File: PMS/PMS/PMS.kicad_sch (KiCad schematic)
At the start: 36 parts, among them IC1 TMCS1107A1BQDRQ1, IC2 ADR3450ARJZ-R7, IC3 TL2575-12IKTTR, J1 XT60PW-M, J2 XT60PW-F, J3 XT60PW-M, J4 XT60PW-F, J5 XT60PW-F, J6 Conn_01x02_Male, U1 ADC101C027CIMK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

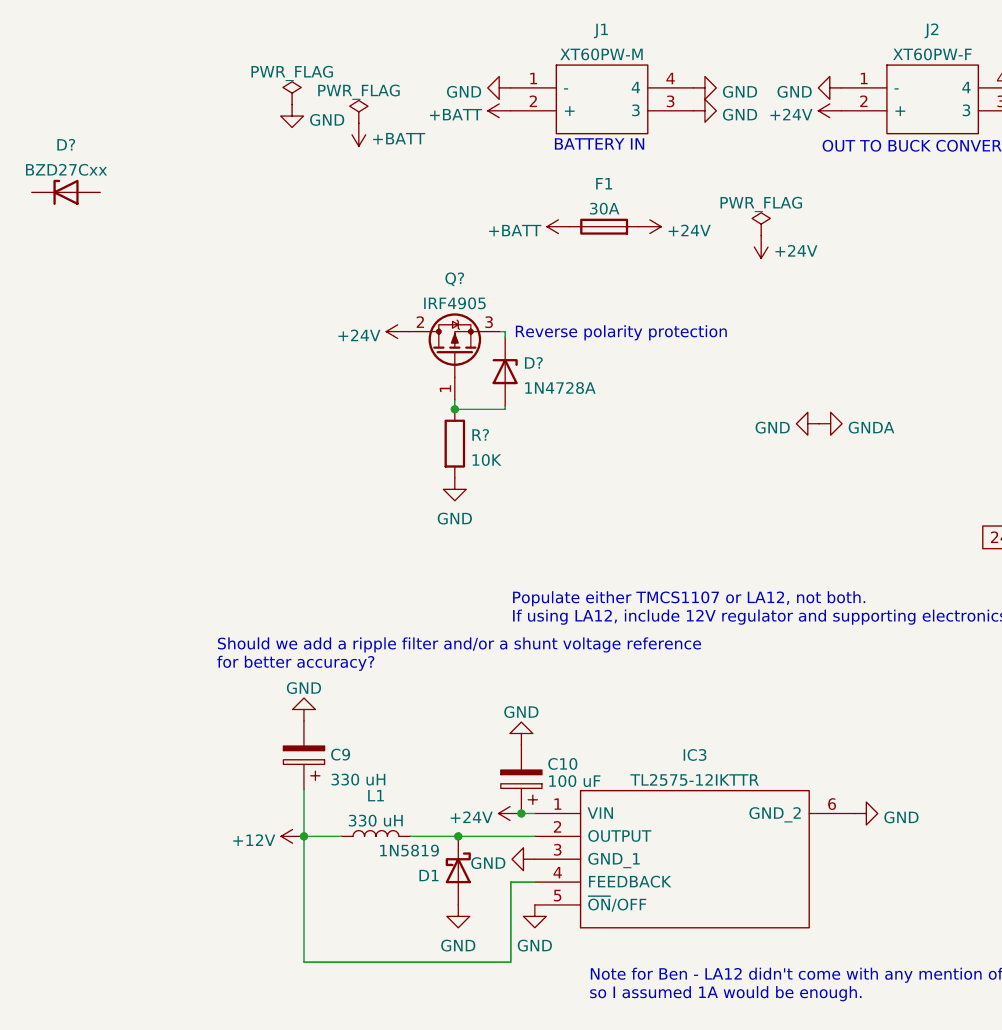
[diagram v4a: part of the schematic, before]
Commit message: cleanup and now ERC compliant
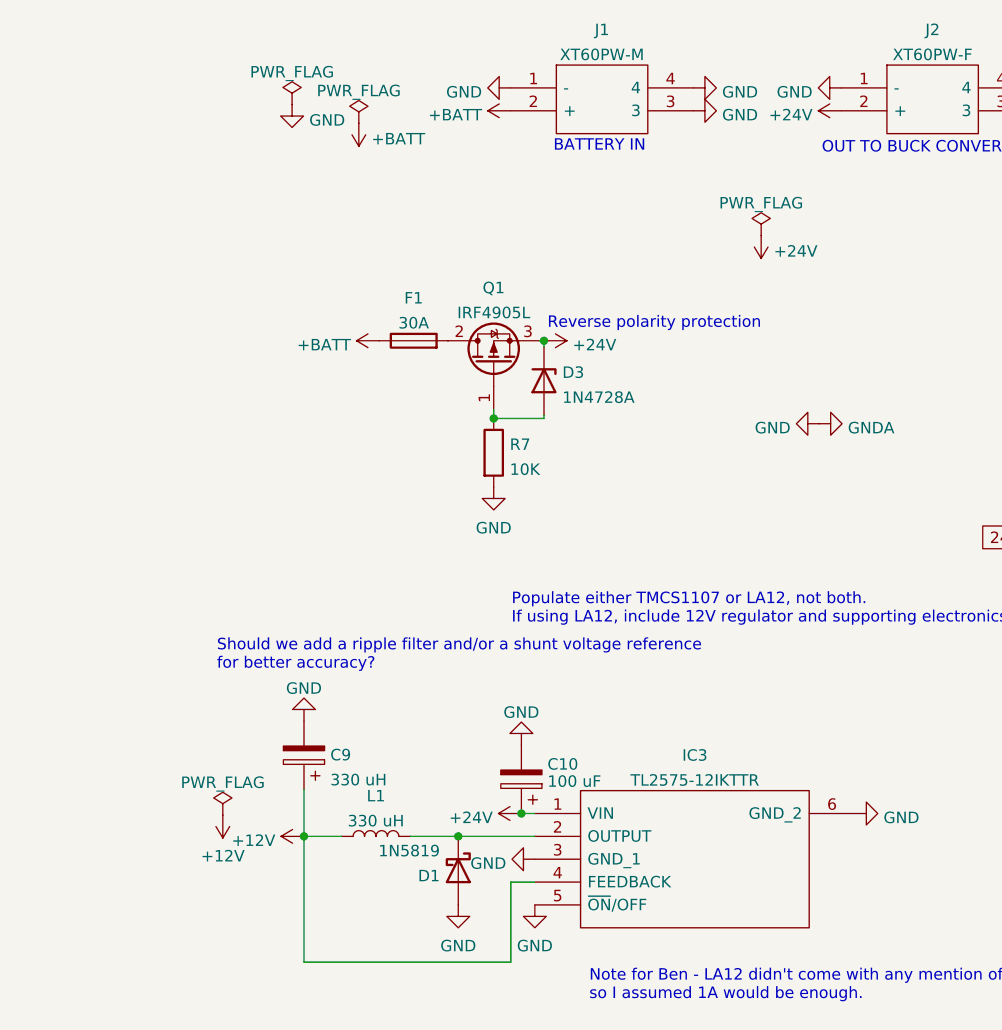
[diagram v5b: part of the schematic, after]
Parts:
- removed D?: BZD27Cxx, Diode_SMD:D_SMF, symbol Diode:BZD27Cxx
- Q1: renamed from Q?; value IRF4905 -> IRF4905L; footprint Package_TO_SOT_THT:TO-220-3_Vertical -> Package_TO_SOT_THT:TO-262-3-1EP_Horizontal_TabDown
- gave numbers to parts that had none: 2
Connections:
- net +24V: now also D3.1 (K), Q1.3 (S); no longer F1.2, Q1.2 (D)
- new net: F1.2, Q1.2 (D)
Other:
- moved on the sheet: D3, F1, Q1, R7

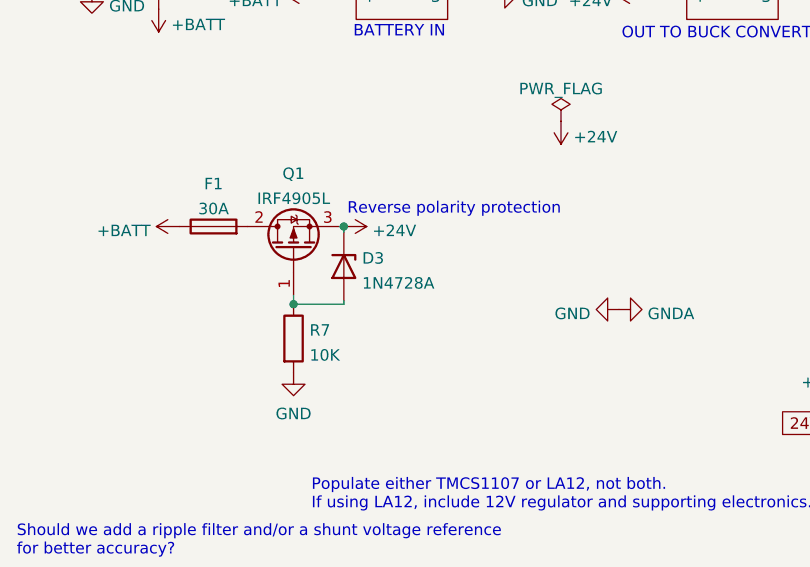
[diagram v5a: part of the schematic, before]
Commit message: switched to the correct zener diode
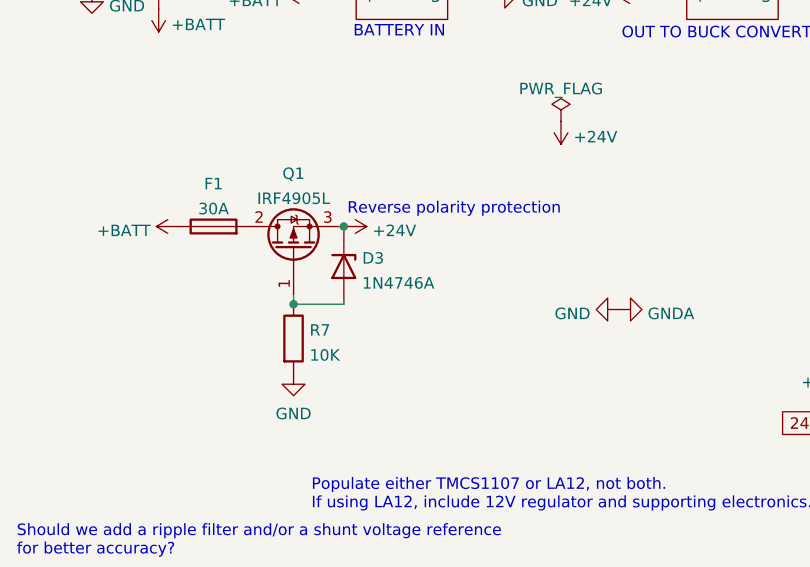
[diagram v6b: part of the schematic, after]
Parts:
- D3: value 1N4728A -> 1N4746A
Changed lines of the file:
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@@
       (effects (font (size 1.27 1.27)) (justify left))
     )
-    (property "Value" "1N4728A" (id 1) (at 58.42 66.6366 90)
+    (property "Value" "1N4746A" (id 1) (at 58.42 66.6366 90)
       (effects (font (size 1.27 1.27)) (justify left))
     )
@@
     )
     (path "/8c58b9c6-42fa-43ad-a456-e387b2c947c3"
-      (reference "D3") (unit 1) (value "1N4728A") (footprint "Diode_THT:D_DO-41_SOD81_P10.16mm_Horizontal")
+      (reference "D3") (unit 1) (value "1N4746A") (footprint "Diode_THT:D_DO-41_SOD81_P10.16mm_Horizontal")
     )
     (path "/f7d7bb3d-3174-4f8d-bddb-cbcecab3f605"

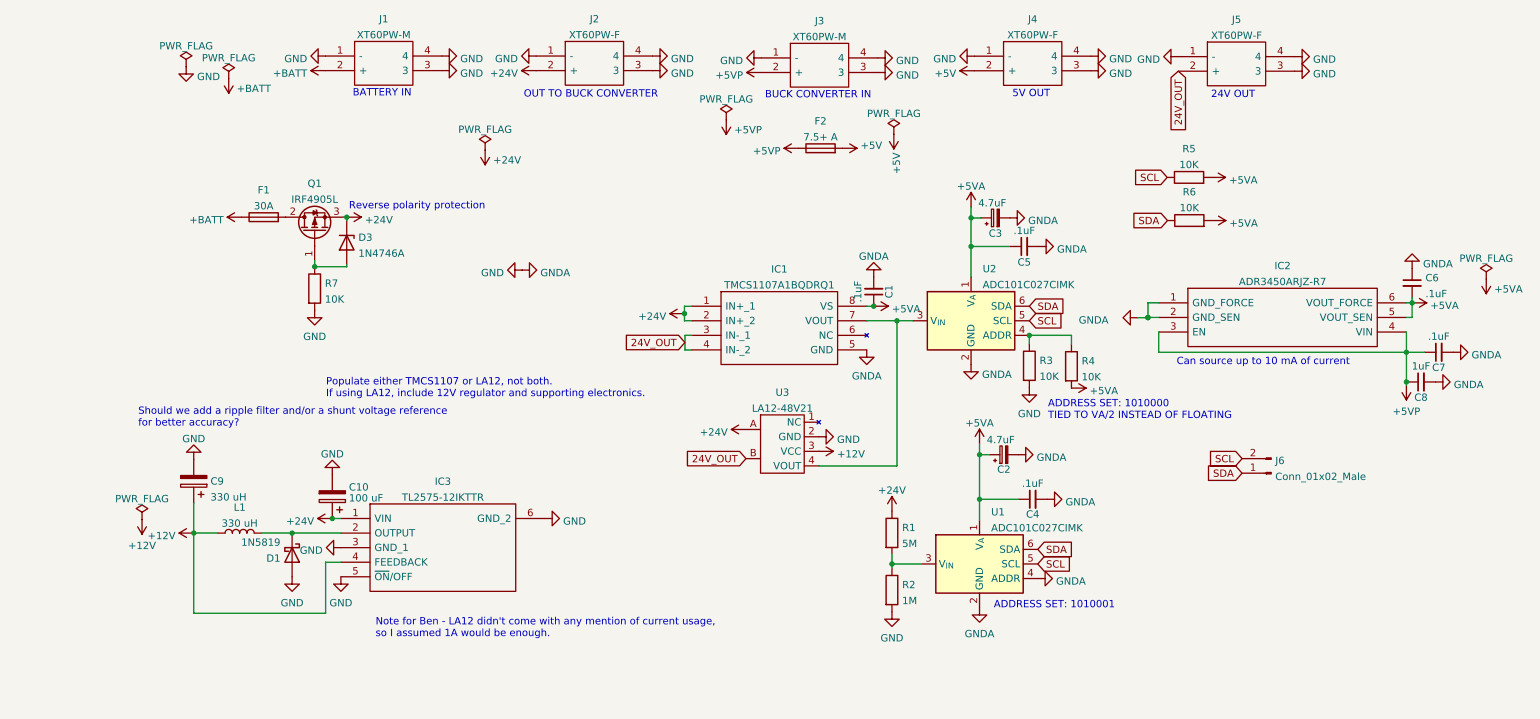
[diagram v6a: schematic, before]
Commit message: Associated footprints to components
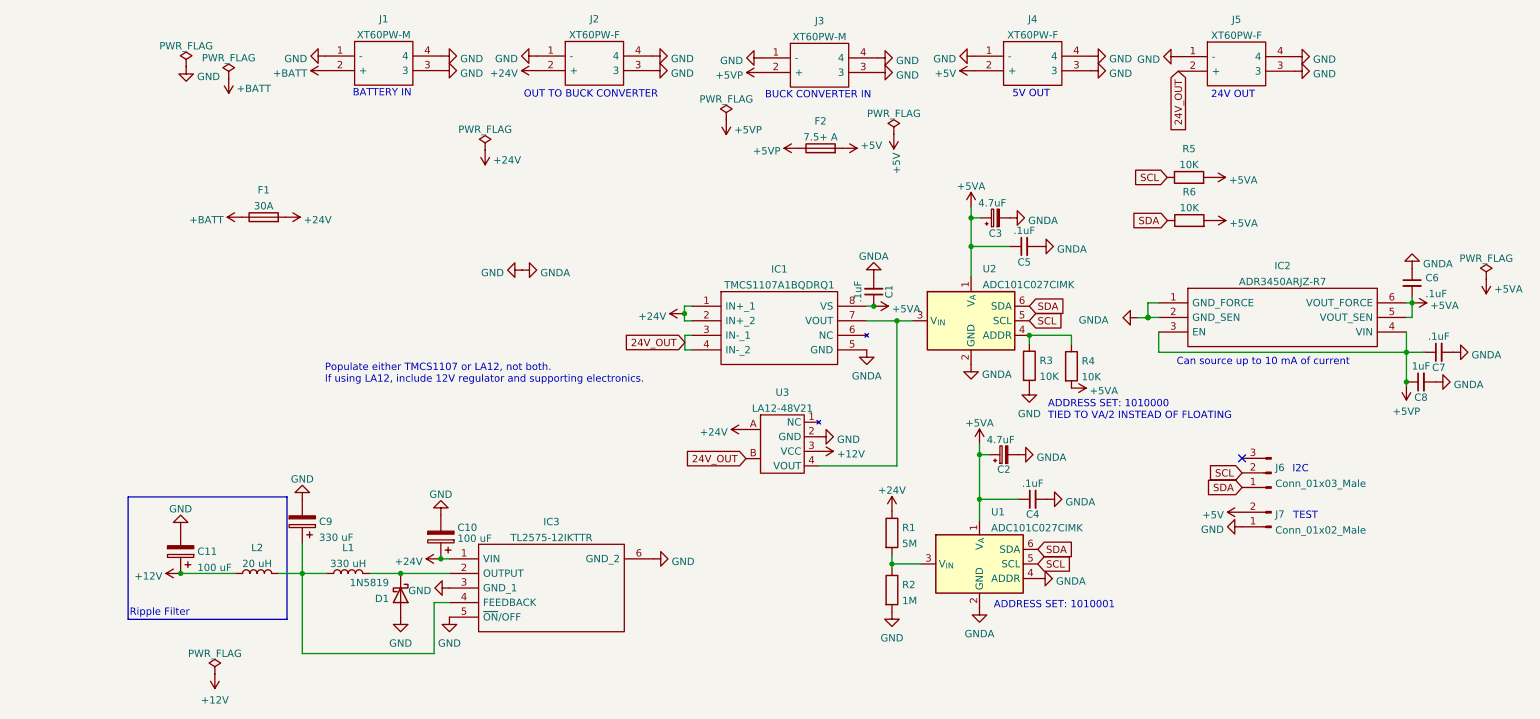
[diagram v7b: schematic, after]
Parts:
- removed D3: 1N4746A, Diode_THT:D_DO-41_SOD81_P10.16mm_Horizontal, symbol Diode:1N47xxA
- removed J6: Conn_01x02_Male, Connector_Molex:Molex_KK-254_AE-6410-02A_1x02_P2.54mm_Vertical, symbol Connector:Conn_01x02_Male
- removed Q1: IRF4905L, Package_TO_SOT_THT:TO-262-3-1EP_Horizontal_TabDown, symbol Transistor_FET:IRF4905
- removed R7: 10K, symbol Device:R
- added C11: 100 uF, Capacitor_SMD:CP_Elec_10x10.5, symbol Device:C_Polarized
- added J6: Conn_01x03_Male, Connector_JST:JST_XH_B3B-XH-AM_1x03_P2.50mm_Vertical, symbol Connector:Conn_01x03_Male
- added J7: Conn_01x02_Male, Connector_JST:JST_XH_B2B-XH-AM_1x02_P2.50mm_Vertical, symbol Connector:Conn_01x02_Male
- added L2: 20 uH, Inductor_SMD:L_Bourns_SRN6045TA, symbol Device:L
- C1, C4, C5, C6, C7, C8: footprint (none) -> Capacitor_SMD:C_0805_2012Metric_Pad1.18x1.45mm_HandSolder
- C10: footprint (none) -> Capacitor_SMD:CP_Elec_10x10.5
- C2, C3: footprint (none) -> Capacitor_Tantalum_SMD:CP_EIA-3216-18_Kemet-A_Pad1.58x1.35mm_HandSolder
- C9: value 330 uH -> 330 uF; footprint (none) -> Capacitor_SMD:CP_Elec_8x6.5
- F1, F2: footprint (none) -> LIB_3576:3576
- L1: footprint (none) -> Inductor_SMD:L_Bourns_SRR1210A
- R1, R2, R3, R4, R5, R6: footprint (none) -> Resistor_SMD:R_0805_2012Metric_Pad1.20x1.40mm_HandSolder
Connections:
- net +12V: now also C11.1, L2.1; no longer C9.1, IC3.4 (FEEDBACK), L1.1
- net +24V: now also F1.2
- net +5V: now also J7.2 (Pin_2)
- net GND: now also C11.2, J7.1 (Pin_1)
- net SCL: now also J6.2 (Pin_2)
- net SDA: now also J6.1 (Pin_1)
- new net: C9.1, IC3.4 (FEEDBACK), L1.1, L2.2
- no-connect marks 0 -> 1
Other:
- note added: "I2C"
- note added: "Ripple Filter"
- note added: "TEST"
- note removed: "Note for Ben - LA12 didn't come with any mention of current usage, so I assumed 1A would be enough."
- note removed: "Reverse polarity protection"
- note removed: "Should we add a ripple filter and/or a shunt voltage reference for better accuracy?"
- moved on the sheet: C10, C9, D1, IC3, L1

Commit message: adding BOM PMS.csv
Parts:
- added J8: Conn_01x02_Male, Connector_JST:JST_XH_B2B-XH-AM_1x02_P2.50mm_Vertical, symbol Connector:Conn_01x02_Male
- C1, C4, C5, C6, C7: DigiKey Part Number (none) -> 399-C0805C104M5RAC7800TR-ND
- C10, C11: DigiKey Part Number (none) -> 399-EDK107M025A9LAATR-ND
- C2, C3: DigiKey Part Number (none) -> 399-3696-1-ND
- C8: DigiKey Part Number (none) -> 399-15436-2-ND
- C9: DigiKey Part Number (none) -> 399-20528-2-ND
- D1: DigiKey Part Number (none) -> 1N5819-E3/54GICT-ND
- F1, F2: DigiKey Part Number (none) -> 36-3576-ND
- IC1: DigiKey Part Number (none) -> 296-TMCS1107A1BQDRQ1TR-ND
- IC2: DigiKey Part Number (none) -> 505-ADR3450ARJZ-R7TR-ND
- IC3: DigiKey Part Number (none) -> 296-21495-2-ND
- J1, J2, J3, J4, J5: TME Part Number (none) -> XT60PW-M
- J6: DigiKey Part Number (none) -> 455-2231-ND
- J7: DigiKey Part Number (none) -> 455-2247-ND
- L1: DigiKey Part Number (none) -> SRR1210-331MTR-ND
- L2: value 20 uH -> 22 uH; DigiKey Part Number (none) -> SRN6045TA-220MTR-ND
- R1: value 5M -> 10M; DigiKey Part Number (none) -> CR0805-JW-106ELFTR-ND
- R2: value 1M -> 2M; footprint Resistor_SMD:R_0805_2012Metric_Pad1.20x1.40mm_HandSolder -> Resistor_SMD:R_0603_1608Metric_Pad0.98x0.95mm_HandSolder; DigiKey Part Number (none) -> CR0603-JW-205ELFTR-ND
- R3, R4: value 10K -> 1M; DigiKey Part Number (none) -> CR0805-JW-105ELFTR-ND
- R5, R6: DigiKey Part Number (none) -> CR0805-JW-103ELFTR-ND
- U1, U2: DigiKey Part Number (none) -> ADC101C027CIMK/NOPBTR-ND
- U3: DigiKey Part Number (none) -> 399-19401-ND
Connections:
- net +12V: now also J8.2 (Pin_2)
- net GND: now also J8.1 (Pin_1)
